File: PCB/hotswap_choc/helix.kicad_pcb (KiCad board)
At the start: 2 copper layers, 135.1 x 94 mm, 124 parts, among them J1 MJ-4PP-9, P1 CONN_01X01, P2 CONN_01X01, P3 OLED, P4 LED, SW1 SW_PUSH, SW10 SW_PUSH, SW11 SW_PUSH, SW12 SW_PUSH, SW13 SW_PUSH, SW14 SW_PUSH, SW15 SW_PUSH, SW16 SW_PUSH, SW17 SW_PUSH, SW18 SW_PUSH, SW19 SW_PUSH, SW2 SW_PUSH, SW20 SW_PUSH, SW21 SW_PUSH, SW22 SW_PUSH, SW23 SW_PUSH, SW24 SW_PUSH, SW25 SW_PUSH, SW26 SW_PUSH, SW27 SW_PUSH, SW28 SW_PUSH, SW29 SW_PUSH, SW3 SW_PUSH, SW30 SW_PUSH, SW31 SW_PUSH, SW32 SW_PUSH, SW33 Reset, SW4 SW_PUSH, SW5 SW_PUSH, SW6 SW_PUSH, SW7 SW_PUSH, SW8 SW_PUSH, SW9 SW_PUSH, U1 ProMicro, U10 SK6812mini, U11 SK6812mini, U12 SK6812mini, U13 SK6812mini, U14 SK6812mini, U15 SK6812mini, U16 SK6812mini, U17 SK6812mini, U18 SK6812mini, U19 SK6812mini, U2 SK6812mini, U20 SK6812mini, U21 SK6812mini, U22 SK6812mini, U23 SK6812mini, U24 SK6812mini, U25 SK6812mini, U26 SK6812mini, U27 SK6812mini, U28 SK6812mini, U29 SK6812mini, U3 SK6812mini, U30 SK6812mini, U31 SK6812mini, U32 SK6812mini, U33 SK6812mini, U4 SK6812mini, U5 SK6812mini, U6 SK6812mini, U7 SK6812mini, U8 SK6812mini, U9 SK6812mini

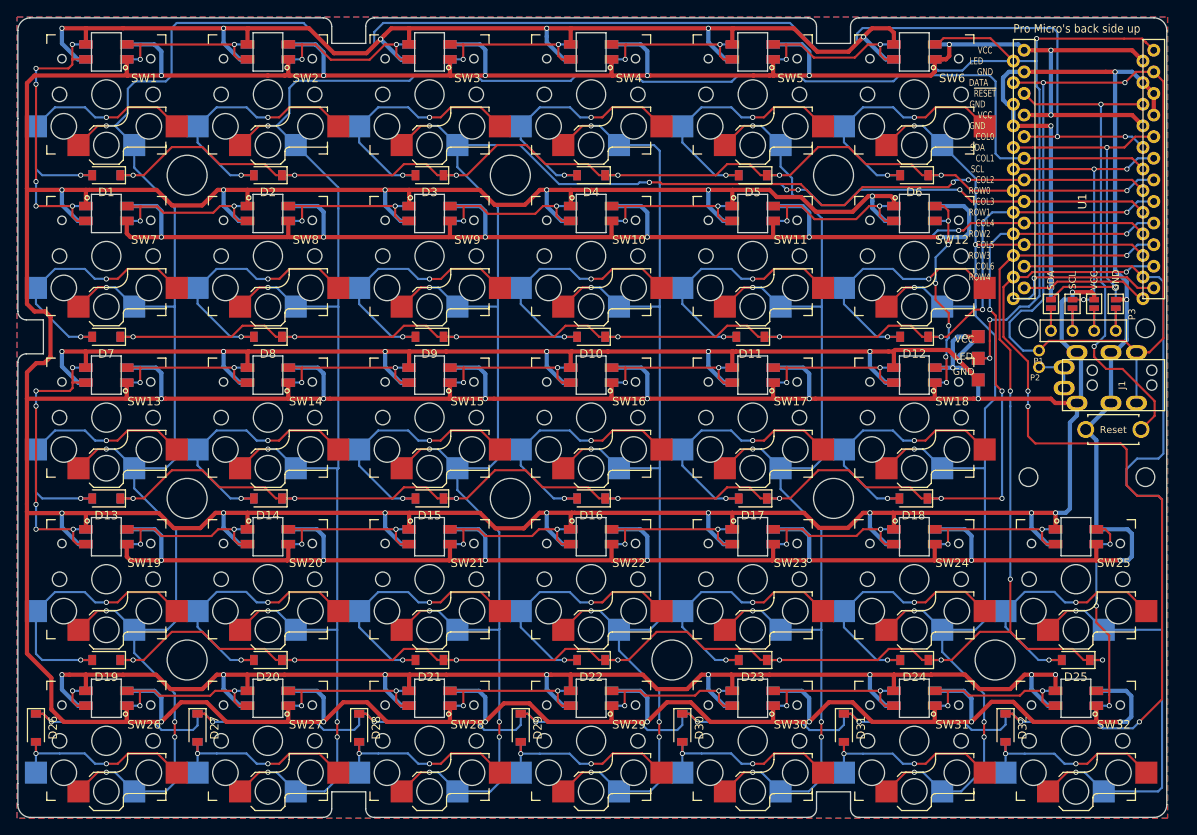
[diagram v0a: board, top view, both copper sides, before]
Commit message: Update of PCB with reassignment of Pad1
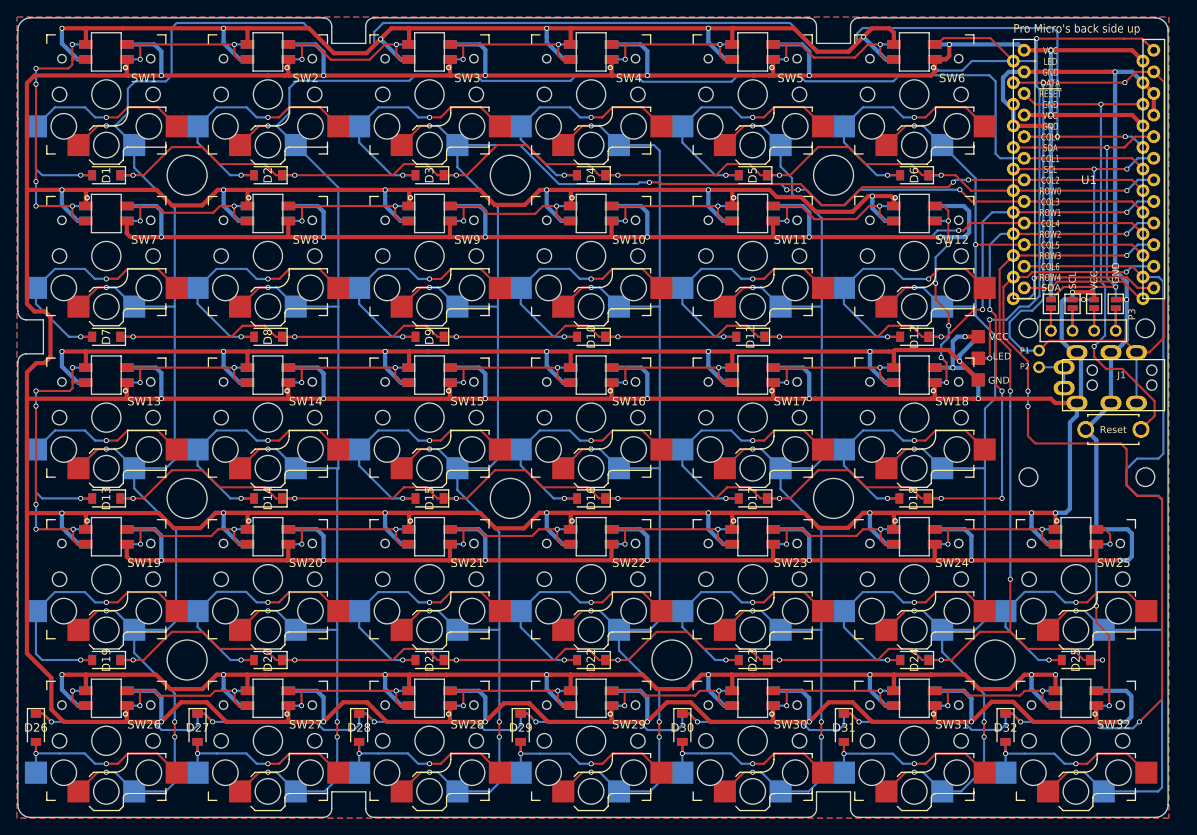
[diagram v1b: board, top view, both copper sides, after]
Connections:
- P1 pad 1: Net-(P1-Pad1) -> data
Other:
- board size 135.1 x 94 mm -> 135.2 x 94 mm
- board text removed: "R1"
- board text removed: "R2"

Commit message: Added I2C resistors and updated gerbers
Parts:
- added R1: 10k, Resistor_SMD:R_0805_2012Metric, B.Cu at (208.0, 49.0)
- added R1: 10k, Resistor_SMD:R_0805_2012Metric, F.Cu at (208.0, 49.0)
- added R2: 10k, Resistor_SMD:R_0805_2012Metric, B.Cu at (206.8, 52.8)
- added R2: 10k, Resistor_SMD:R_0805_2012Metric, F.Cu at (206.8, 52.8)
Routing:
- net VCC: track 1034.1 -> 1047.3 mm, vias 38 -> 41
- net /SDA: track 44.0 -> 56.8 mm, vias 2 -> 3
- net /SCL: track 34.9 -> 46.6 mm, vias 3 -> 4

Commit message: Update of silkscreen
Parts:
- added G***: LOGO, Logos:IronMan_small, B.Cu at (196.5, 99.5)
- added G***: LOGO, Logos:IronMan_small, F.Cu at (196.5, 99.5)
- added G***: Helix_logo_small, Logos:Helix_logo_small, B.Cu at (201.3, 92.4)
- added G***: Helix_logo_small, Logos:Helix_logo_small, F.Cu at (201.3, 92.4)
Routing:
- net col5: track 160.1 -> 163.4 mm
- net GND: vias 37 -> 40
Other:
- board text added: "HS Choc Edition"
- board text added: "PCB Designed by Cipulot"

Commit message: Updated silkscreen and logos
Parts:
- added G***: LOGO, Logos:IronMan_helix, F.Cu at (149.0, 91.0)
- added G***: LOGO, Logos:Single_flower_helix, B.Cu at (138.4, 89.2)
- turned G*** to 180 degrees

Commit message: Update
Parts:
- removed the G*** at (149.0, 91.0)
- added G***: LOGO, Logos:Double_flower_helix, F.Cu at (146.7, 92.2)
- SW1, SW10, SW11, SW12, SW13, SW14, SW15, SW16, SW17, SW18, SW19, SW2, SW20, SW21, SW22, SW23, SW24, SW25, SW26, SW27, SW28, SW29, SW3, SW30, SW31, SW32, SW4, SW5, SW6, SW7, SW8, SW9: footprint Keyswitches:Kailh_socket_PG1350_reversible_LEFT -> Keyswitches:Kailh_socket_PG1350_reversible_LEFT_nosilkangle

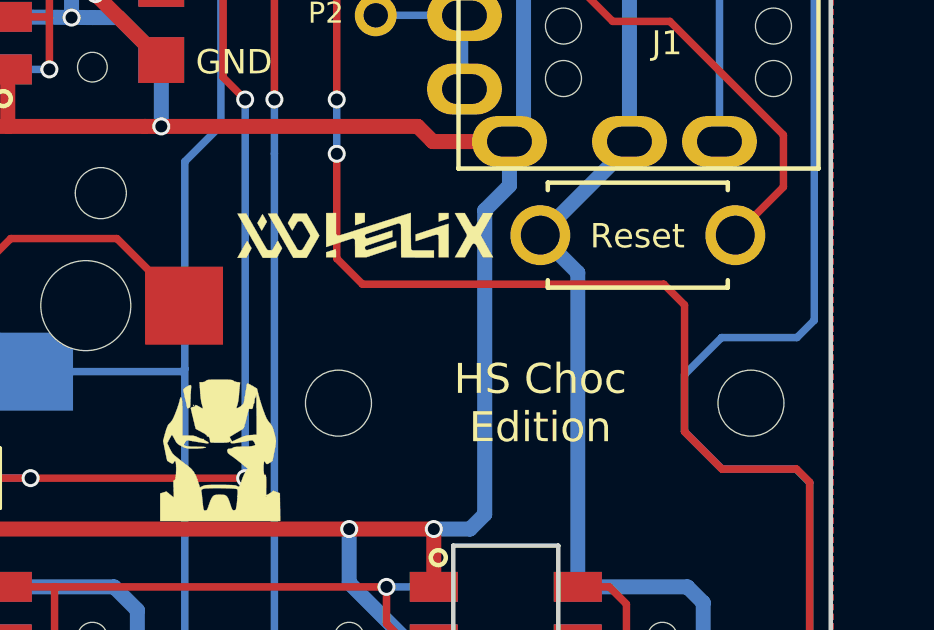
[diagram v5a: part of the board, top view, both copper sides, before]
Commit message: Update pcb silkscreen
Added silkscreen for crediting original Helix creator: @MakotoKurauchi .
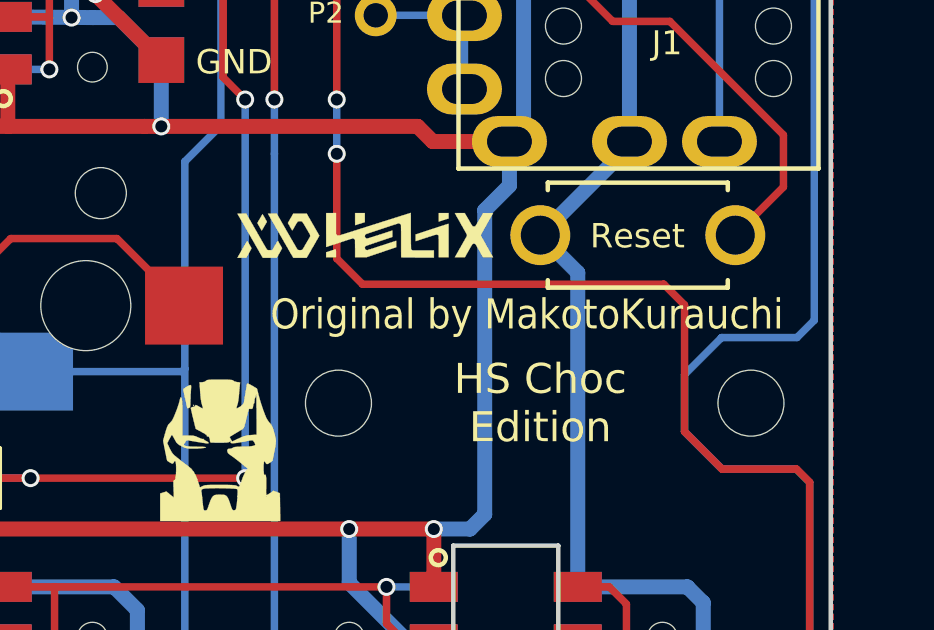
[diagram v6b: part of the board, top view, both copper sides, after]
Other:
- board text added: "Original by MakotoKurauchi"
